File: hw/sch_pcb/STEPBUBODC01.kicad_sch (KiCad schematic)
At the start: 20 parts, among them J1 HEADER_1x03, J2 HEADER_2x03_PARALLEL, J3 HEADER_1x03, J4 HEADER_1x03, J5 HEADER_2x03_PARALLEL, J6 HEADER_2x03_PARALLEL, U1 TPS631000DRLR

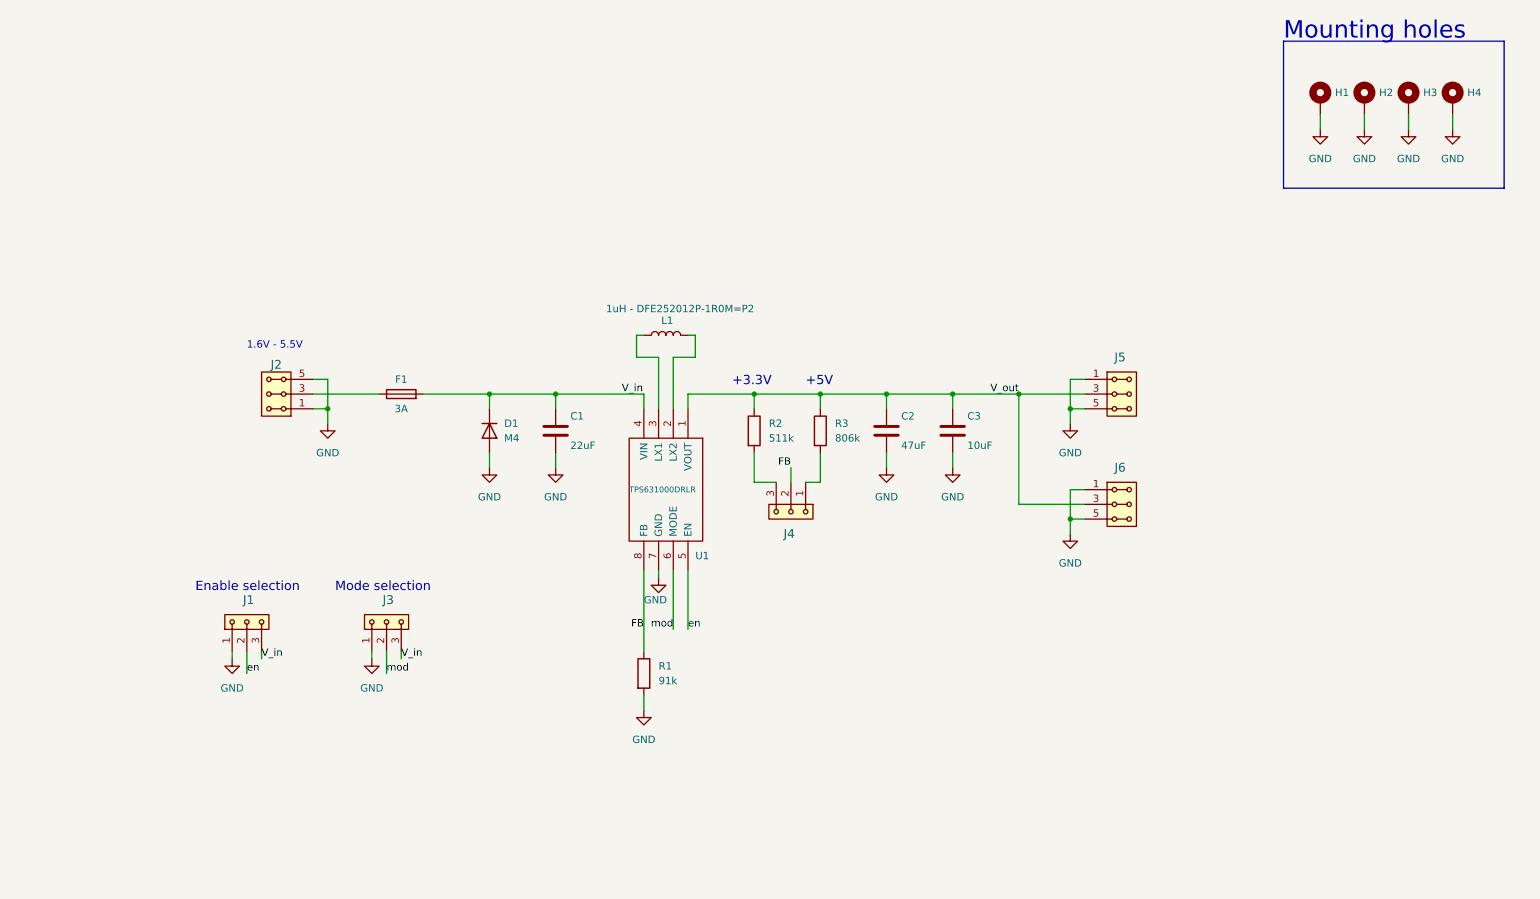
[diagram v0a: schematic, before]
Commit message: Improvements in schematics and layout, solve: #1, #2, #4
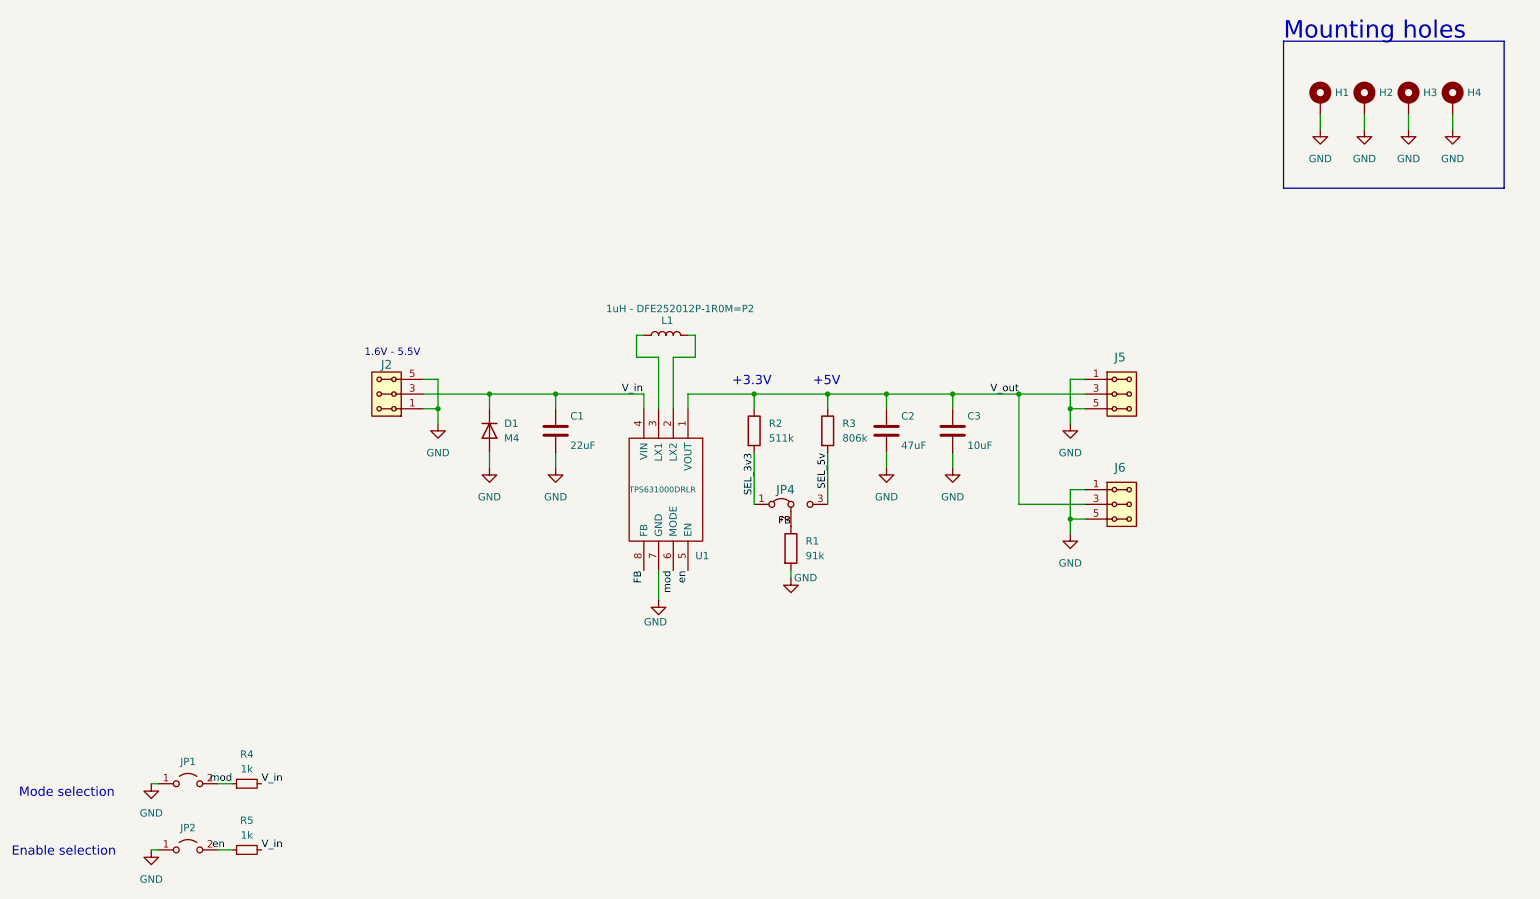
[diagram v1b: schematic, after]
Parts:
- removed F1: 3A, symbol Device:Fuse
- removed J1, J3: HEADER_1x03, Mlab_Pin_Headers:Straight_1x03, symbol MLAB_HEADER:HEADER_1x03
- added JP1, JP2: Jumper_2_Open, Connector_PinHeader_2.54mm:PinHeader_1x02_P2.54mm_Vertical, symbol Jumper:Jumper_2_Open
- added R4, R5: 1k, Resistor_SMD:R_0805_2012Metric, symbol Device:R_Small
- C1, C2, C3: footprint Mlab_C:SMD-0805 -> Capacitor_SMD:C_0805_2012Metric
- D1: footprint (none) -> Diode_SMD:D_SMA
- J2, J5, J6: footprint Mlab_Pin_Headers:Straight_2x03 -> Connector_PinHeader_2.54mm:PinHeader_2x03_P2.54mm_Vertical
- JP4: renamed from J4; footprint Mlab_Pin_Headers:Straight_1x03 -> Connector_PinHeader_2.54mm:PinHeader_1x03_P2.54mm_Vertical; symbol MLAB_HEADER:HEADER_1x03 -> Jumper:Jumper_3_Bridged12
- R1, R2, R3: footprint Mlab_R:SMD-0805 -> Resistor_SMD:R_0805_2012Metric
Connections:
- net GND: now also JP1.1 (A), JP2.1 (A)
- net V_in: now also J2.3, J2.4, R4.2, R5.2
- net en: now also JP2.2 (B), R5.1
- net mod: now also JP1.2 (B), R4.1
- net SEL_3v3: now reaches JP4.1 (A)
- net SEL_3v3: now also R2.2; no longer R3.2
- net SEL_5v: now reaches JP4.3 (B)
- net SEL_5v: now also R3.2; no longer R2.2
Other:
- moved on the sheet: J2, R1, R3

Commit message: add fidu, check layout, drc, update ust_id
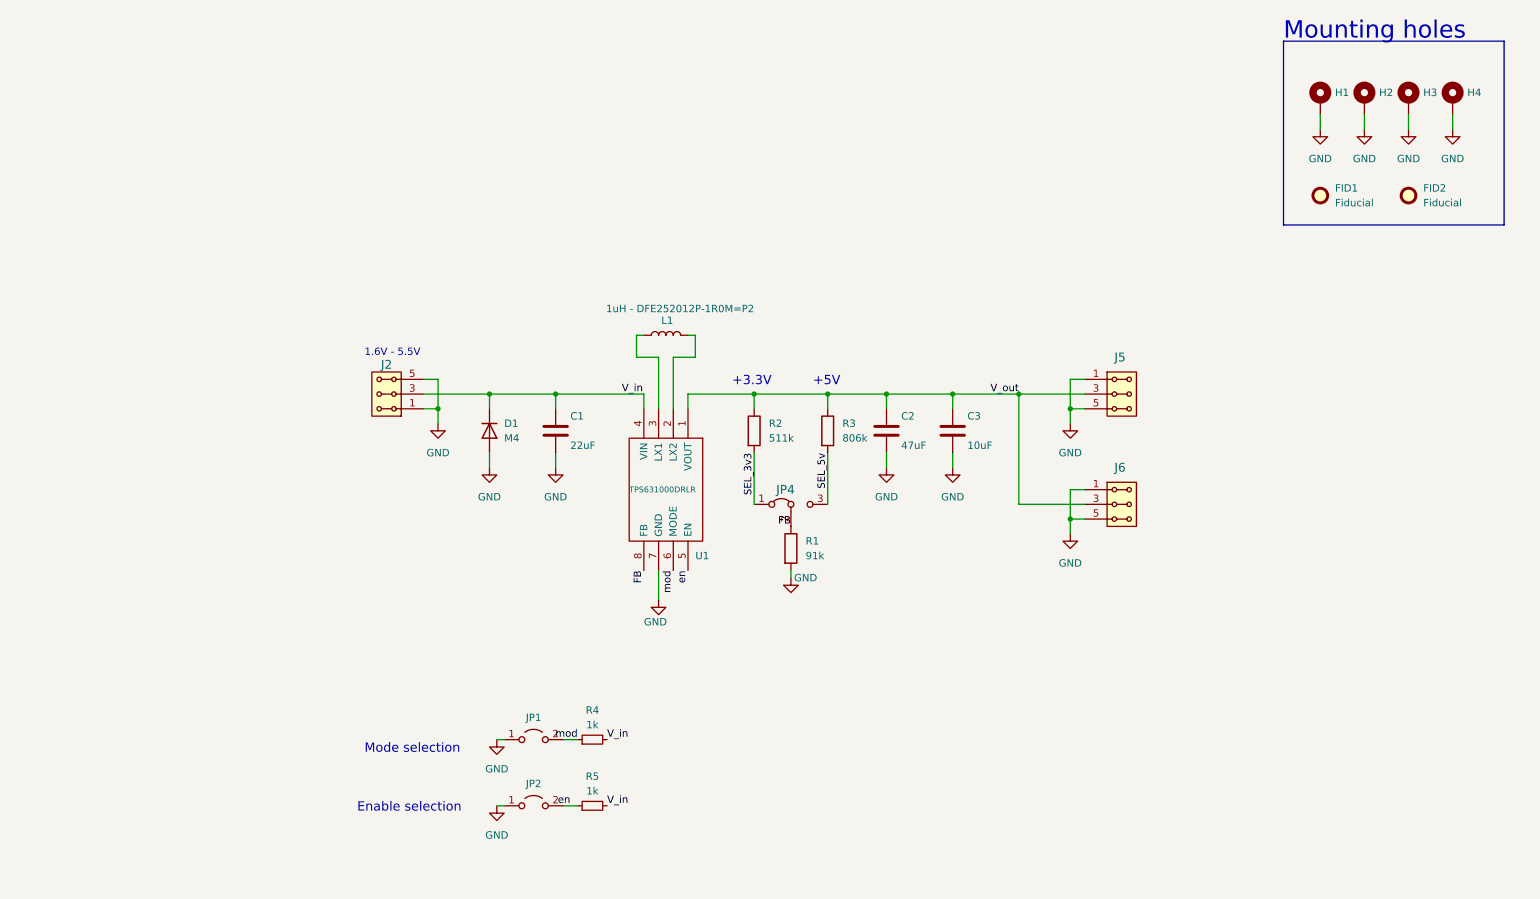
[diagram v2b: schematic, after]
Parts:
- added FID1, FID2: Fiducial, Fiducial:Fiducial_1mm_Mask2mm, symbol Mechanical:Fiducial
- C1: Height (none) -> 650b58f1462c6d9e7205463b
- C2: Height (none) -> 5c70984812875079b91f8bbf
- C3: Height (none) -> 5c70984712875079b91f8b53
- D1: Height (none) -> 5c70984512875079b91f88ac
- L1: Height (none) -> 650b5977462c6d9e72054656
- R1: Height (none) -> 650b59ec462c6d9e72054677
- R2: Height (none) -> 650b5a43462c6d9e7205468e
- R3: Height (none) -> 650b5abb462c6d9e720546b8
- R4, R5: Height (none) -> 5c70984512875079b91f898c
- U1: Height 0.6 -> 63de5ae4ae0b2d5aa05e2714
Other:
- moved on the sheet: JP1, JP2, R4, R5

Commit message: change USTID field
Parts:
- C1: Height 650b58f1462c6d9e7205463b -> (none); UST_ID (none) -> 650b58f1462c6d9e7205463b
- C2: Height 5c70984812875079b91f8bbf -> (none); UST_ID (none) -> 5c70984812875079b91f8bbf
- C3: Height 5c70984712875079b91f8b53 -> (none); UST_ID (none) -> 5c70984712875079b91f8b53
- D1: Height 5c70984512875079b91f88ac -> (none); UST_ID (none) -> 5c70984512875079b91f88ac
- L1: Height 650b5977462c6d9e72054656 -> (none); UST_ID (none) -> 650b5977462c6d9e72054656
- R1: Height 650b59ec462c6d9e72054677 -> (none); UST_ID (none) -> 650b59ec462c6d9e72054677
- R2: Height 650b5a43462c6d9e7205468e -> (none); UST_ID (none) -> 650b5a43462c6d9e7205468e
- R3: Height 650b5abb462c6d9e720546b8 -> (none); UST_ID (none) -> 650b5abb462c6d9e720546b8
- R4, R5: Height 5c70984512875079b91f898c -> (none); UST_ID (none) -> 5c70984512875079b91f898c
- U1: Height 63de5ae4ae0b2d5aa05e2714 -> (none); UST_ID (none) -> 63de5ae4ae0b2d5aa05e2714
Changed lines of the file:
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@@
       (effects (font (size 1.27 1.27)) hide)
     )
-    (property "Height" "650b59ec462c6d9e72054677" (at 158.75 106.68 0)
-      (effects (font (size 1.27 1.27)) hide)
-    )
-    (property "UST_ID" "" (at 158.75 106.68 0)
+    (property "Height" "" (at 158.75 106.68 0)
+      (effects (font (size 1.27 1.27)) hide)
+    )
+    (property "UST_ID" "650b59ec462c6d9e72054677" (at 158.75 106.68 0)
       (effects (font (size 1.27 1.27)) hide)
     )
@@
       (effects (font (size 1.27 1.27)) hide)
     )
-    (property "UST_ID" "" (at 165.1 86.36 0)
-      (effects (font (size 1.27 1.27)) hide)
-    )
-    (property "Height" "650b5abb462c6d9e720546b8" (at 165.1 86.36 0)
+    (property "UST_ID" "650b5abb462c6d9e720546b8" (at 165.1 86.36 0)
+      (effects (font (size 1.27 1.27)) hide)
+    )
+    (property "Height" "" (at 165.1 86.36 0)
       (effects (font (size 1.27 1.27)) hide)
     )
@@
       (effects (font (size 1.27 1.27)) hide)
     )
-    (property "Height" "5c70984712875079b91f8b53" (at 186.69 86.36 0)
-      (effects (font (size 1.27 1.27)) hide)
-    )
-    (property "UST_ID" "" (at 186.69 86.36 0)
+    (property "Height" "" (at 186.69 86.36 0)
+      (effects (font (size 1.27 1.27)) hide)
+    )
+    (property "UST_ID" "5c70984712875079b91f8b53" (at 186.69 86.36 0)
       (effects (font (size 1.27 1.27)) hide)
     )
@@
       (effects (font (size 1.27 1.27)) hide)
     )
-    (property "UST_ID" "" (at 137.16 69.85 0)
-      (effects (font (size 1.27 1.27)) hide)
-    )
-    (property "Height" "650b5977462c6d9e72054656" (at 137.16 69.85 0)
+    (property "UST_ID" "650b5977462c6d9e72054656" (at 137.16 69.85 0)
+      (effects (font (size 1.27 1.27)) hide)
+    )
+    (property "Height" "" (at 137.16 69.85 0)
       (effects (font (size 1.27 1.27)) hide)
     )
@@
       (effects (font (size 1.27 1.27)) (justify left) hide)
     )
-    (property "Height" "63de5ae4ae0b2d5aa05e2714" (at 135.89 106.68 0)
+    (property "Height" "" (at 135.89 106.68 0)
       (effects (font (size 1.27 1.27)) (justify left) hide)
     )
@@
       (effects (font (size 1.27 1.27)) (justify left) hide)
     )
-    (property "UST_ID" "" (at 140.97 82.55 0)
+    (property "UST_ID" "63de5ae4ae0b2d5aa05e2714" (at 140.97 82.55 0)
       (effects (font (size 1.27 1.27)) hide)
     )
@@
       (effects (font (size 1.27 1.27)) hide)
     )
-    (property "Height" "5c70984512875079b91f898c" (at 124.46 151.13 0)
-      (effects (font (size 1.27 1.27)) hide)
-    )
-    (property "UST_ID" "" (at 124.46 151.13 0)
+    (property "Height" "" (at 124.46 151.13 0)
+      (effects (font (size 1.27 1.27)) hide)
+    )
+    (property "UST_ID" "5c70984512875079b91f898c" (at 124.46 151.13 0)
       (effects (font (size 1.27 1.27)) hide)
     )
@@
       (effects (font (size 1.27 1.27)) hide)
     )
-    (property "Height" "5c70984512875079b91f88ac" (at 106.68 86.36 0)
-      (effects (font (size 1.27 1.27)) hide)
-    )
-    (property "UST_ID" "" (at 106.68 86.36 0)
+    (property "Height" "" (at 106.68 86.36 0)
+      (effects (font (size 1.27 1.27)) hide)
+    )
+    (property "UST_ID" "5c70984512875079b91f88ac" (at 106.68 86.36 0)
       (effects (font (size 1.27 1.27)) hide)
     )
@@
       (effects (font (size 1.27 1.27)) hide)
     )
-    (property "Height" "5c70984512875079b91f898c" (at 124.46 139.7 0)
-      (effects (font (size 1.27 1.27)) hide)
-    )
-    (property "UST_ID" "" (at 124.46 139.7 0)
+    (property "Height" "" (at 124.46 139.7 0)
+      (effects (font (size 1.27 1.27)) hide)
+    )
+    (property "UST_ID" "5c70984512875079b91f898c" (at 124.46 139.7 0)
       (effects (font (size 1.27 1.27)) hide)
     )
@@
       (effects (font (size 1.27 1.27)) hide)
     )
-    (property "Height" "5c70984812875079b91f8bbf" (at 175.26 86.36 0)
-      (effects (font (size 1.27 1.27)) hide)
-    )
-    (property "UST_ID" "" (at 175.26 86.36 0)
+    (property "Height" "" (at 175.26 86.36 0)
+      (effects (font (size 1.27 1.27)) hide)
+    )
+    (property "UST_ID" "5c70984812875079b91f8bbf" (at 175.26 86.36 0)
       (effects (font (size 1.27 1.27)) hide)
     )
@@
       (effects (font (size 1.27 1.27)) hide)
     )
-    (property "UST_ID" "" (at 118.11 86.36 0)
-      (effects (font (size 1.27 1.27)) hide)
-    )
-    (property "Height" "650b58f1462c6d9e7205463b" (at 118.11 86.36 0)
+    (property "UST_ID" "650b58f1462c6d9e7205463b" (at 118.11 86.36 0)
+      (effects (font (size 1.27 1.27)) hide)
+    )
+    (property "Height" "" (at 118.11 86.36 0)
       (effects (font (size 1.27 1.27)) hide)
     )
@@
       (effects (font (size 1.27 1.27)) hide)
     )
-    (property "UST_ID" "" (at 152.4 86.36 0)
-      (effects (font (size 1.27 1.27)) hide)
-    )
-    (property "Height" "650b5a43462c6d9e7205468e" (at 152.4 86.36 0)
-      (effects (font (size 1.27 1.27)) hide)
-    )
+    (property "UST_ID" "650b5a43462c6d9e7205468e" (at 152.4 86.36 0)
+      (effects (font (size 1.27 1.27)) hide)
+    )
+    (property "Height" "" (at 152.4 86.36 0)
+      (effects (font (size 1.27 1.27)) hide)
+    )

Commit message: Kontrola a opravy pred vyrobou
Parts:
- U1: footprint KiCad:SOTFL50P160X60-8N -> Mlab_IO:TPS631000
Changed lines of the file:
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@@
       (effects (font (size 1 1)) (justify left))
     )
-    (property "Footprint" "KiCad:SOTFL50P160X60-8N" (at 143.51 106.68 0)
+    (property "Footprint" "Mlab_IO:TPS631000" (at 143.51 106.68 0)
       (effects (font (size 1.27 1.27)) (justify left) hide)
     )
